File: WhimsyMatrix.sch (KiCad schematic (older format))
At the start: 96 parts, among them K1 KEYSW, K10 KEYSW, K11 KEYSW, K12 KEYSW, K13 KEYSW, K14 KEYSW, K15 KEYSW, K16 KEYSW, K17 KEYSW, K18 KEYSW, K19 KEYSW, K2 KEYSW, K20 KEYSW, K21 KEYSW, K22 KEYSW, K23 KEYSW, K24 KEYSW, K25 KEYSW, K26 KEYSW, K27 KEYSW, K29 KEYSW, K3 KEYSW, K30 KEYSW, K31 KEYSW, K32 KEYSW, K33 KEYSW, K34 KEYSW, K35 KEYSW, K36 KEYSW, K37 KEYSW, K38 KEYSW, K39 KEYSW, K4 KEYSW, K40 KEYSW, K41 KEYSW, K42 KEYSW, K43 KEYSW, K44 KEYSW, K45 KEYSW, K46 KEYSW, K47 KEYSW, K48 KEYSW, K5 KEYSW, K6 KEYSW, K7 KEYSW, K8 KEYSW, K9 KEYSW, SW1 Rotary_Encoder_Switch

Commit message: added elite-c, changed switch matrix to groups, added LED breakout, added off board reset switch, added OLED pins
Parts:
- renumbered D48 to D28, K48 to K28
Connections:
- net col10 is gone; now on net col1: K41.1, K42.1, K43.1, K44.1
- net col11 is gone; now on net col0: K45.1, K46.1, K47.1, SW1.S1
- net col6 is gone; now on net col5: K25.1, K26.1, K27.1
- net col7 is gone; now on net col4: K29.1, K30.1, K31.1, K32.1
- net col8 is gone; now on net col3: K33.1, K34.1, K35.1, K36.1
- net col9 is gone; now on net col2: K37.1, K38.1, K39.1, K40.1
- net col5: now also K28.1
- net row0: no longer D29.1 (K), D33.1 (K), D37.1 (K), D41.1 (K), D45.1 (K)
- net row1: no longer D30.1 (K), D34.1 (K), D38.1 (K), D42.1 (K), D46.1 (K)
- net row2: no longer D31.1 (K), D35.1 (K), D39.1 (K), D43.1 (K), D47.1 (K)
- net row3: no longer D28.1 (K), D32.1 (K), D36.1 (K), D40.1 (K), D44.1 (K)
- net at D28.2 (A): now also K28.2
- new net row4: D29.1 (K), D33.1 (K), D37.1 (K), D41.1 (K), D45.1 (K)
- new net row5: D30.1 (K), D34.1 (K), D38.1 (K), D42.1 (K), D46.1 (K)
- new net row6: D31.1 (K), D35.1 (K), D39.1 (K), D43.1 (K), D47.1 (K)
- new net row7: D28.1 (K), D32.1 (K), D36.1 (K), D40.1 (K), D44.1 (K)
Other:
- moved on the sheet: D1, D10, D11, D12, D13, D14, D15, D16, D17, D18, D19, D2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

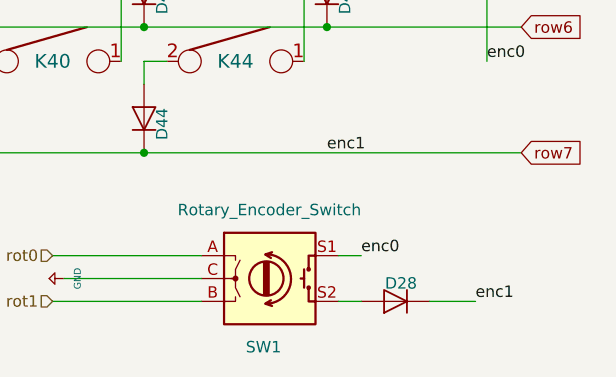
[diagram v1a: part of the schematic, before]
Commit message: duplicate diode (D28) fixed
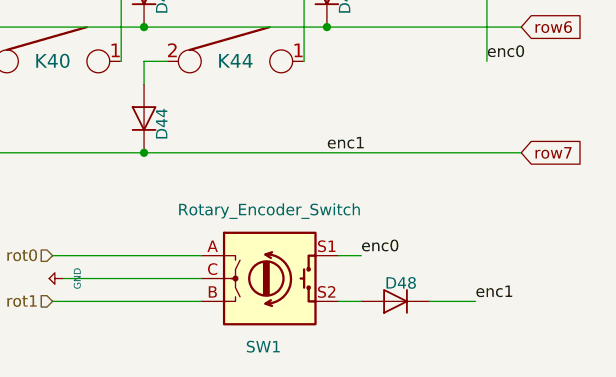
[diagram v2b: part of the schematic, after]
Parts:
- renumbered D28 to D48
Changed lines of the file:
@@
 $EndComp
 $Comp
-L Device:D D28
+L Device:D D48
 U 1 1 5E80A1E9
 P 10200 5500
-F 0 "D28" H 10246 5421 50  0000 R CNN
+F 0 "D48" H 10246 5421 50  0000 R CNN
 F 1 "D" V 10155 5421 50  0001 R CNN
 F 2 "" H 10200 5500 50  0001 C CNN
@@
 $EndComp
 $Comp
-L keyboard_parts:GND #PWR?
+L keyboard_parts:GND #PWR0107
 U 1 1 5E8C39A1
 P 8750 5400
-F 0 "#PWR?" H 8750 5450 20  0001 C CNN
+F 0 "#PWR0107" H 8750 5450 20  0001 C CNN
 F 1 "GND" H 8750 5459 30  0000 C CNN
 F 2 "" H 8750 5400 60  0000 C CNN

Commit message: first layout test
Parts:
- D1, D10, D11, D12, D13, D14, D15, D16, D17, D18, D19, D2, D20, D21, D22, D23, D24, D25, D26, D27, D28, D29, D3, D30, D31, D32, D33, D34, D35, D36, D37, D38, D39, D4, D40, D41, D42, D43, D44, D45, D46, D47, D48, D5, D6, D7, D8, D9: footprint (none) -> SofleKeyboard-footprint:Diode_SOD123
- K1, K10, K11, K12, K13, K14, K15, K16, K17, K18, K19, K2, K20, K21, K22, K23, K25, K26, K27, K28, K29, K3, K30, K31, K32, K33, K34, K35, K36, K37, K38, K39, K4, K40, K41, K42, K43, K44, K45, K46, K47, K5, K6, K7, K8, K9: footprint (none) -> keebs:Mx_Alps_100
- K24: footprint (none) -> keebs:Mx_Alps_200
- SW1: footprint (none) -> SofleKeyboard-footprint:RotaryEncoder_Alps_EC11E-Switch_Vertical_H20mm-keebio_modified

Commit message: properly laid out keys, cut edges
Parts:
- K2, K20, K28, K46: footprint keebs:Mx_Alps_100 -> keebs:Mx_Alps_125
- K3, K45: footprint keebs:Mx_Alps_100 -> keebs:Mx_Alps_150
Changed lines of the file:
@@
 F 0 "K28" H 6300 4450 60  0000 C CNN
 F 1 "KEYSW" H 6300 4350 60  0001 C CNN
-F 2 "keebs:Mx_Alps_100" H 6300 4450 60  0001 C CNN
+F 2 "keebs:Mx_Alps_125" H 6300 4450 60  0001 C CNN
 F 3 "" H 6300 4450 60  0000 C CNN
 	1    6300 4450
@@
 F 0 "K20" H 4700 4450 60  0000 C CNN
 F 1 "KEYSW" H 4700 4350 60  0001 C CNN
-F 2 "keebs:Mx_Alps_100" H 4700 4450 60  0001 C CNN
+F 2 "keebs:Mx_Alps_125" H 4700 4450 60  0001 C CNN
 F 3 "" H 4700 4450 60  0000 C CNN
 	1    4700 4450
@@
 F 0 "K3" H 1500 3900 60  0000 C CNN
 F 1 "KEYSW" H 1500 3800 60  0001 C CNN
-F 2 "keebs:Mx_Alps_100" H 1500 3900 60  0001 C CNN
+F 2 "keebs:Mx_Alps_150" H 1500 3900 60  0001 C CNN
 F 3 "" H 1500 3900 60  0000 C CNN
 	1    1500 3900
@@
 F 0 "K46" H 10300 3300 60  0000 C CNN
 F 1 "KEYSW" H 10300 3200 60  0001 C CNN
-F 2 "keebs:Mx_Alps_100" H 10300 3300 60  0001 C CNN
+F 2 "keebs:Mx_Alps_125" H 10300 3300 60  0001 C CNN
 F 3 "" H 10300 3300 60  0000 C CNN
 	1    10300 3300
@@
 F 0 "K2" H 1500 3300 60  0000 C CNN
 F 1 "KEYSW" H 1500 3200 60  0001 C CNN
-F 2 "keebs:Mx_Alps_100" H 1500 3300 60  0001 C CNN
+F 2 "keebs:Mx_Alps_125" H 1500 3300 60  0001 C CNN
 F 3 "" H 1500 3300 60  0000 C CNN
 	1    1500 3300
@@
 F 0 "K45" H 10300 2700 60  0000 C CNN
 F 1 "KEYSW" H 10300 2600 60  0001 C CNN
-F 2 "keebs:Mx_Alps_100" H 10300 2700 60  0001 C CNN
+F 2 "keebs:Mx_Alps_150" H 10300 2700 60  0001 C CNN
 F 3 "" H 10300 2700 60  0000 C CNN
 	1    10300 2700

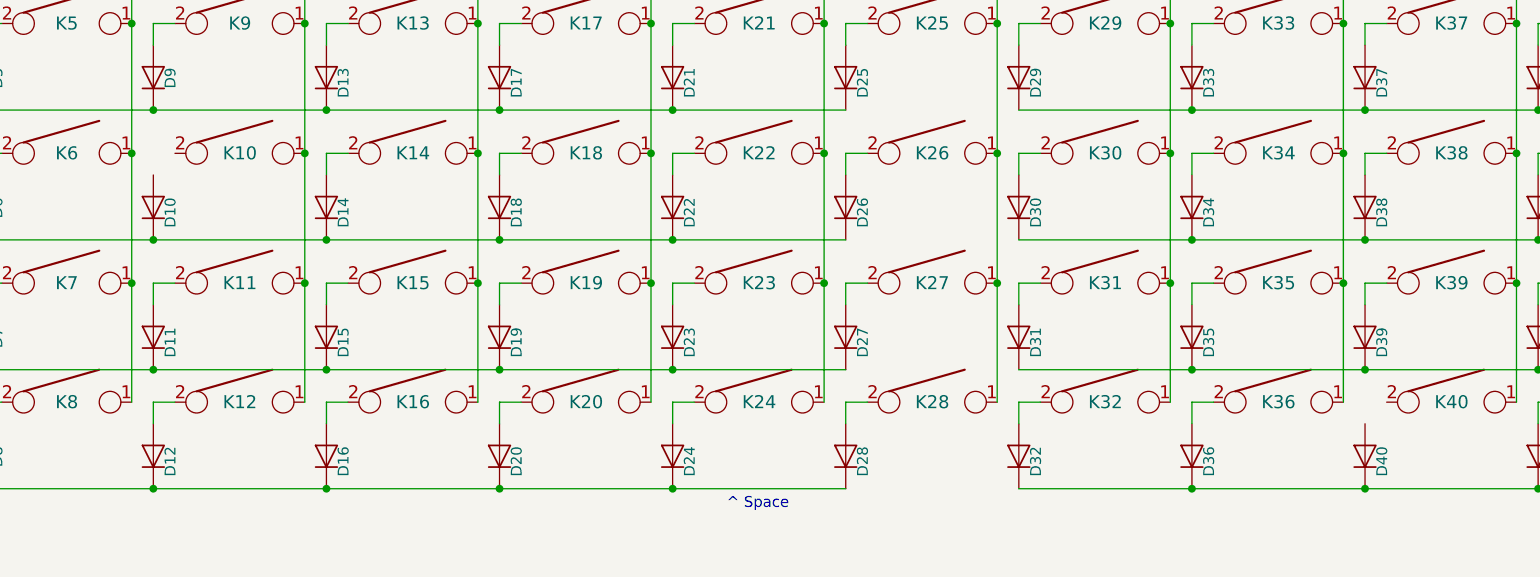
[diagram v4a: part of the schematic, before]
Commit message: started routing traces, finishing rev0.1
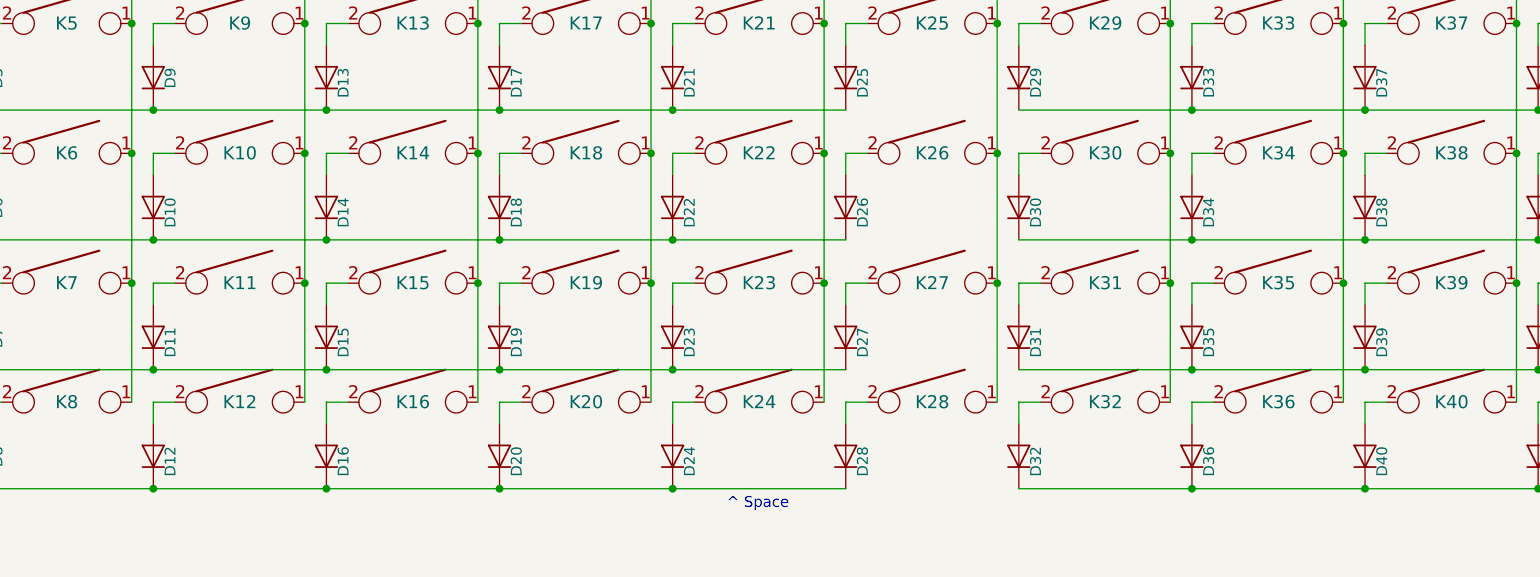
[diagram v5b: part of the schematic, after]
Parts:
- D1, D10, D11, D12, D13, D14, D15, D16, D17, D18, D19, D2, D20, D21, D22, D23, D24, D25, D26, D27, D28, D29, D3, D30, D31, D32, D33, D34, D35, D36, D37, D38, D39, D4, D40, D41, D42, D43, D44, D45, D46, D47, D48, D5, D6, D7, D8, D9: footprint SofleKeyboard-footprint:Diode_SOD123 -> Keebio-Parts:Diode-Hybrid-Back
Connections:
- net at D40.2 (A): now also K40.2
- net at D10.2 (A): now also K10.2

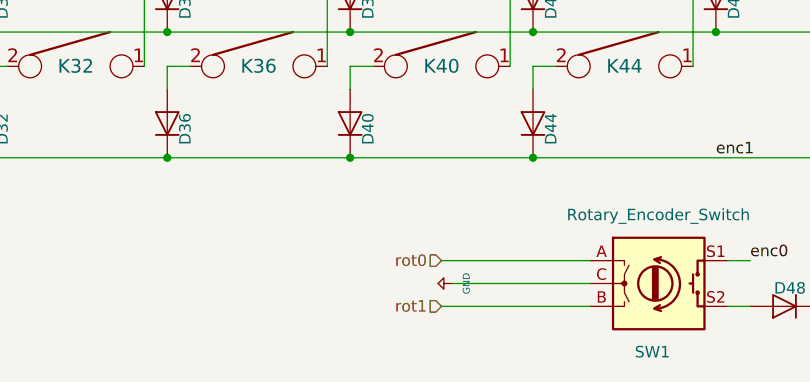
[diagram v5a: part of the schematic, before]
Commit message: better routing, columns, rows and via's to connect to the elite c
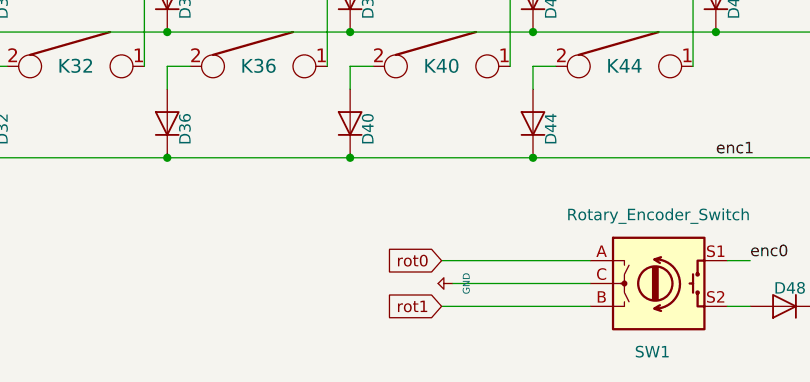
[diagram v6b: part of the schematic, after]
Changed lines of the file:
@@
 encoding utf-8
 Sheet 2 2
-Title "Whimsey"
-Date "2020-03-03"
-Rev "A"
+Title "Whimsy"
+Date "2020-03-05"
+Rev "0.1"
 Comp "Prkns"
 Comment1 ""
@@
 	0    1    1    0
 $EndComp
-Text HLabel 8700 5500 0    50   Input ~ 0
-rot1
-Text HLabel 8700 5300 0    50   Input ~ 0
-rot0
 Connection ~ 5100 4850
 Text Label 10600 4450 0    50   ~ 0
@@
 Wire Wire Line
 	2700 3300 2800 3300
+Text GLabel 8700 5300 0    50   Input ~ 0
+rot0
+Text GLabel 8700 5500 0    50   Input ~ 0
+rot1
 $EndSCHEMATC

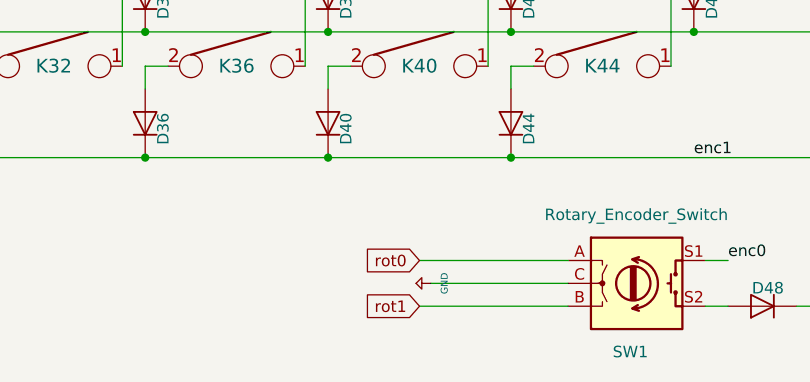
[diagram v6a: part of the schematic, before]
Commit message: gnd pins were not working as inteded, solder mask was a little off, fixed overall matrix, tightened the schematic to make it more logical
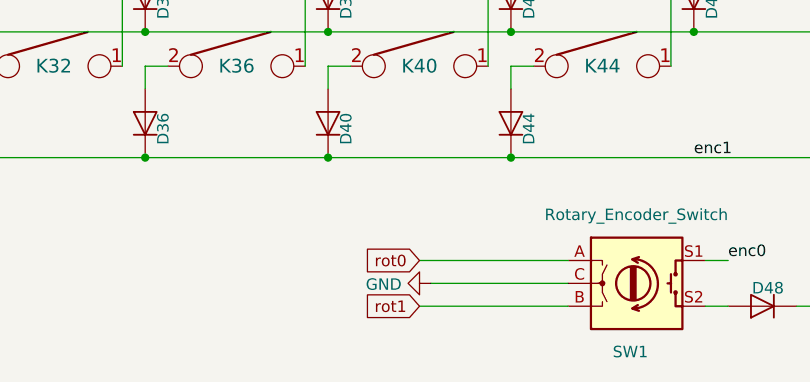
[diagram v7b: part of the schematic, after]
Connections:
- net +5V renamed GND
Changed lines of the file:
@@
 	-1   0    0    1
-$EndComp
-$Comp
-L keyboard_parts:GND #PWR0107
-U 1 1 5E8C39A1
-P 8750 5400
-F 0 "#PWR0107" H 8750 5450 20  0001 C CNN
-F 1 "GND" H 8750 5459 30  0000 C CNN
-F 2 "" H 8750 5400 60  0000 C CNN
-F 3 "" H 8750 5400 60  0000 C CNN
-	1    8750 5400
-	0    1    1    0
 $EndComp
 Connection ~ 5100 4850
@@
 Text GLabel 8700 5500 0    50   Input ~ 0
 rot1
+$Comp
+L power:GND #PWR0106
+U 1 1 5E66BE2A
+P 8750 5400
+F 0 "#PWR0106" H 8750 5150 50  0001 C CNN
+F 1 "GND" V 8755 5272 50  0000 R CNN
+F 2 "" H 8750 5400 50  0001 C CNN
+F 3 "" H 8750 5400 50  0001 C CNN
+	1    8750 5400
+	0    1    1    0
+$EndComp
 $EndSCHEMATC
